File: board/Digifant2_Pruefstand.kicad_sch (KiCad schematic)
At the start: 58 parts, among them J0 VW ECU HARNESS, J1 12V BENCH IN, J2 IDLE VALVE N71, J3 OLED / UI I2C, Q1 2N7002, Q2 P-MOS -30V >=5A, Q3 2N7002, Q5 2N7002, SW1 PUSH, SW2 PUSH, SW3 PUSH, U1 INA226 (0x40), U2 MCP4728 (0x60), U3 INA226 (0x41), U4 AD9833, U5 Raspberry Pi Pico, U6 TS5A3159A, U7 TS5A3159A, U8 TS5A3159A, Y1 25MHz

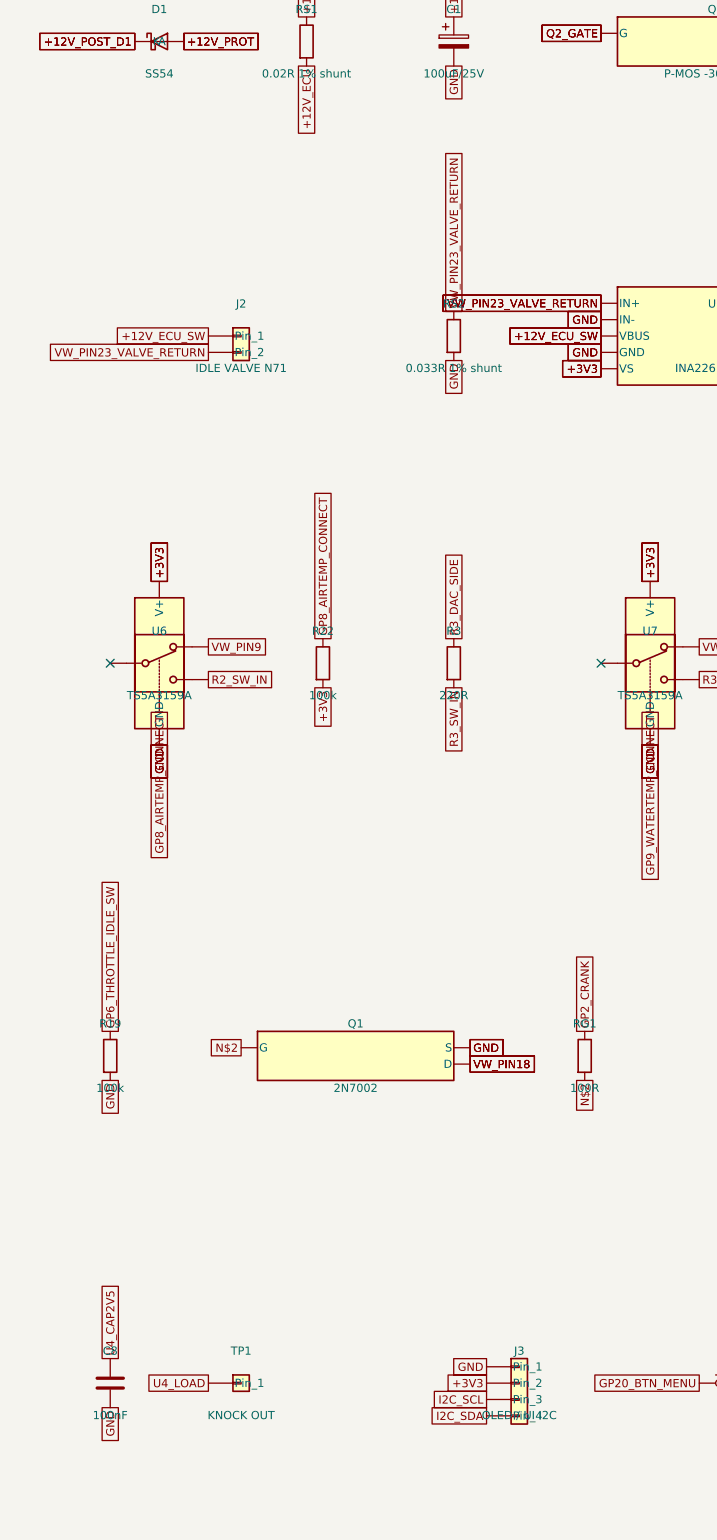
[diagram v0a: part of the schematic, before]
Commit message: Fix RS2's parallel ground path and give the knock output a real path out
Two of the three genuinely-open findings from USE_CASES.md:

1. RS2 (idle-valve shunt) sat as a separate tap to GND, in parallel with
   the ECU's own low-side driver on VW-23 -- both reached the same shared
   GND, so return current split between RS2 and the ECU's internal switch,
   and U3 only ever measured whatever fraction happened through RS2.
   Understated the true current, worst exactly when the ECU driver was on.
   Fixed: RS2 is now truly in series (valve -> RS2 -> VW-23), so 100% of
   the return current crosses it. U3's IN+/IN- assignment was swapped
   (IN+ keeps the net that already had a routed path to J0, IN- takes the
   new sense-side net) purely to minimize how much existing routing needed
   to change -- sign of the current reading is a firmware convention
   either way.

2. AD9833 knock output dead-ended at a single test pad with no path out.
   J0 is already full (15/15 positions; VW-4/5/7 were never broken out
   there), so this needed a separate small tap, same idea as J2 for the
   idle valve. A proper 2-pin JST connector was tried first (matching
   J2's style) but every placement attempt shorted a different existing
   net -- this corner of the board is threaded with +12V_ECU_SW,
   VW_PIN10/11/12, and GP8/GP9/GP13/GP26 on both layers. Used two small
   bare test pads (TP1 signal, TP2 ground, same footprint as the original
   TP1) instead, which fit where the connector wouldn't.

Both required real topology changes, not just added parts -- updated the
circuit source AND spliced the corresponding net-label renames into the
committed schematic (not just the PCB), otherwise a future PCB-from-
schematic sync would have silently reverted the RS2 fix.

One new residual, same class as the existing U1/U3/RS1/RS2 pocket: U3
pin 9's own local GND-mesh neighbours and its new sense-net connection
both need to route through the same tight spot. Tried by hand and via
Freerouting f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
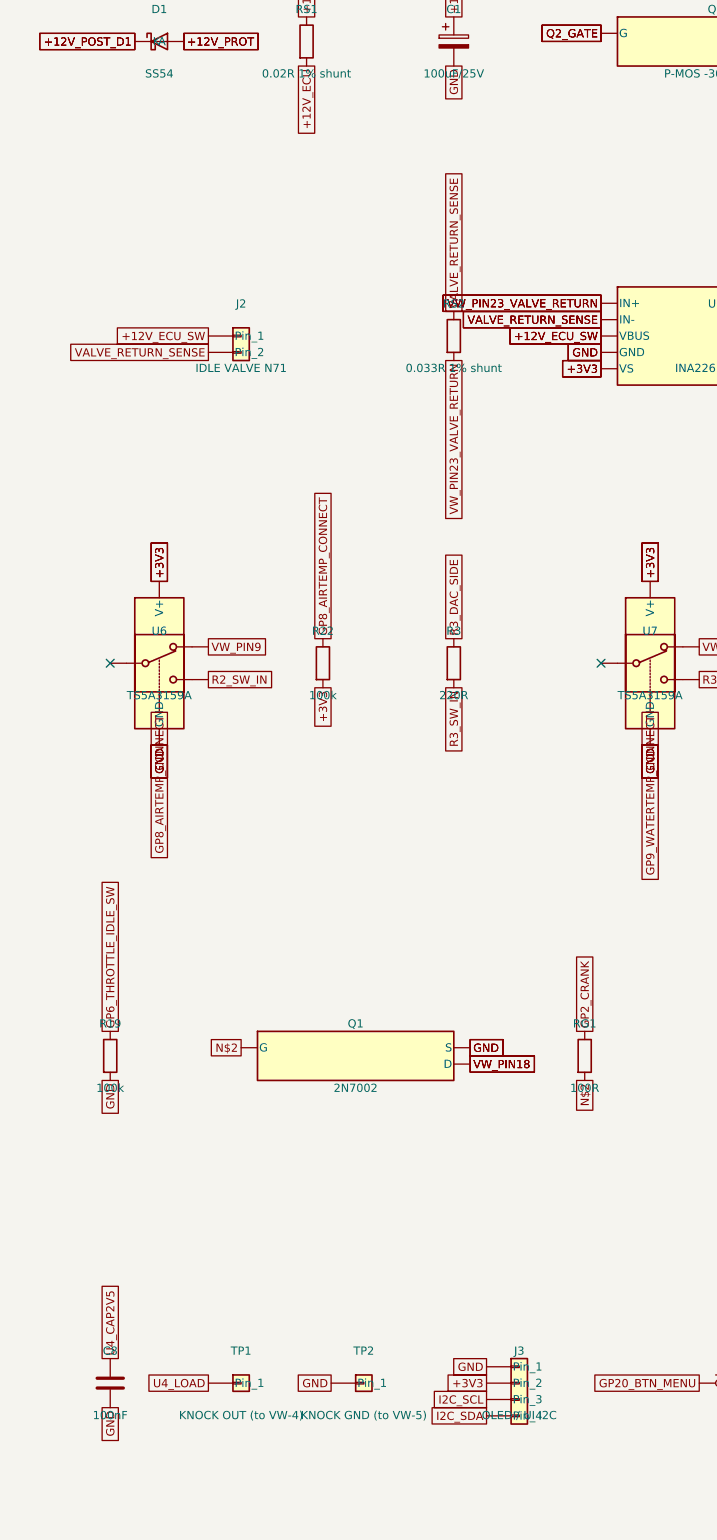
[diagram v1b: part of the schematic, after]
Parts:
- added TP2: KNOCK GND (to VW-5), TestPoint:TestPoint_Pad_D1.5mm, symbol Connector_Generic:Conn_01x01
- TP1: value KNOCK OUT -> KNOCK OUT (to VW-4)
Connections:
- net GND: now also TP2.1 (Pin_1); no longer RS2.2, U3.9 (IN-)
- net VW_PIN23_VALVE_RETURN: now also RS2.2; no longer J2.2 (Pin_2), RS2.1
- new net VALVE_RETURN_SENSE: J2.2 (Pin_2), RS2.1, U3.9 (IN-)
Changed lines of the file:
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@@
 		(property
 			"Value"
-			"KNOCK OUT"
+			"KNOCK OUT (to VW-4)"
 			(at 58.42 314.88 0)
 			(effects
@@
 			)
 		)
+		(symbol
+			(lib_id Connector_Generic:Conn_01x01)
+			(at 77.47 309.88 0)
+			(in_bom yes)
+			(on_board yes)
+			(dnp no)
+			(property
+				"Reference"
+				"TP2"
+				(at 77.47 304.88 0)
+				(effects
+					(font
+						(size 1.27 1.27)
+					)
+				)
+			)
+			(property
+				"Value"
+				"KNOCK GND (to VW-5)"
+				(at 77.47 314.88 0)
+				(effects
+					(font
+						(size 1.27 1.27)
+					)
+				)
+			)
+			(property
+				"Footprint"
+				"TestPoint:TestPoint_Pad_D1.5mm"
+				(at 77.47 319.88 0)
+				(effects
+					(font
+						(size 1.27 1.27)
+					)
+					(hide yes)
+				)
+			)
+			(instances
+				(project
+					"circuit"
+					(path
+						"/"
+						(reference TP2)
+						(unit 1)
+					)
+				)
+				(project
+					"/workspace/digifant2-pruefstand/digifant2_pruefstand_scratch_fix23/digifant2_pruefstand_scratch_fix23"
+					(path
+						"/1d0c82a2-feac-4989-ac41-75dbcafe7445/27b0ed1e-7c83-4569-a3b4-468bc8a85a9f"
+						(reference TP2)
+						(unit 1)
+					)
+				)
+			)
+		)
 	(global_label
 		VW_PIN2
@@
 	)
 	(global_label
-		GND
+		VW_PIN23_VALVE_RETURN
 		(at 91.44 151.13 270)
 		(effects
@@
 	)
 	(global_label
-		GND
+		VALVE_RETURN_SENSE
 		(at 114.30000000000001 144.78 180)
 		(effects
@@
 	)
 	(global_label
-		GND
+		VALVE_RETURN_SENSE
 		(at 114.30000000000001 144.78 180)
 		(effects
@@
 	)
 	(global_label
-		VW_PIN23_VALVE_RETURN
+		VALVE_RETURN_SENSE
 		(at 53.34 149.85999999999999 180)
 		(effects
@@
 	)
 	(global_label
-		VW_PIN23_VALVE_RETURN
+		VALVE_RETURN_SENSE
 		(at 91.44 143.51 90)
 		(effects
@@
 			(effects
 				(font
+					(size 1.27 1.27)
+				)
+				(justify right)
+			)
+		)
+		(global_label
+			GND
+			(at 72.39 309.88 180)
+			(effects
+				(font

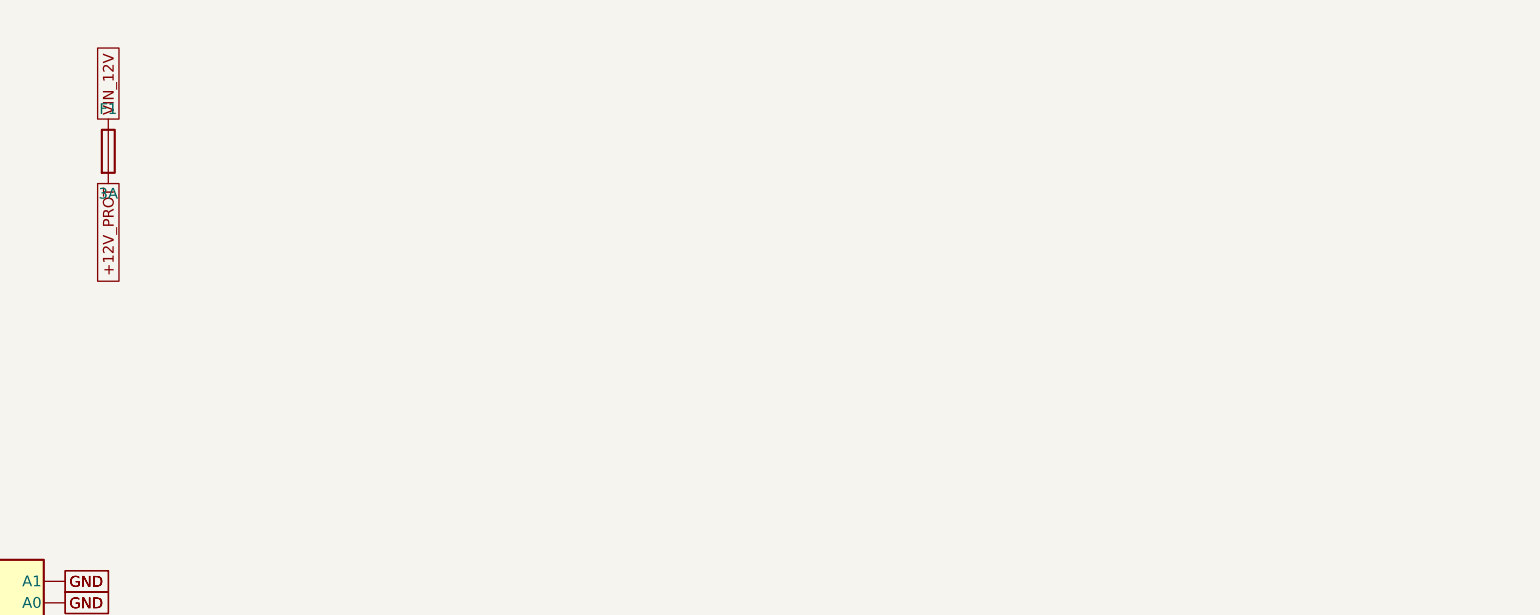
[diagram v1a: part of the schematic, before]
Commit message: Add 12 scope-probe test points (TP3-TP14) for firmware debugging
Bare 1.5mm test pads (same TestPoint_Pad_D1.5mm footprint as the knock
output's TP1/TP2) on the signals most likely to get probed while
debugging: crank drive, idle-switch drive, ignition/injector capture,
the AD9833 SPI bus (CS/SCK/MOSI), the I2C bus (SDA/SCL), the status LED
data line, and both 12V rails (sensed + switched).

Placement used an automated collision check (footprint + track distance)
against the real board, not manual trial and error -- 12 of 13 originally
attempted points cleared on the first or second pass. +3V3 was dropped
after 4 different anchor attempts (3 different Pico pins, then a
decoupling cap elsewhere) all routed through the same congested corridor
near the Pico; not worth forcing given +3V3 is already exposed at many
existing component pins.

Added digifant2_pruefstand.py's debug_test_points() and spliced the
corresponding schematic symbols/labels into the committed schematic
(verified ERC-clean and schematic-PCB parity unchanged from baseline) --
same lesson as the RS2 fix: a PCB-only addition would silently disappear
on the next schematic sync.

One real residual: TP12 (LED data) reopened a shorting_items/clearance
pair against GND. The actual pad-to-pad distances involved are ~2mm --
nowhere near a real clearance violation -- so the true conflict is
somewhere along the newly-routed copper itself, not locatable precisely
by script. Left for the same manual-nudge treatment as this board's
other tight pockets; KiCad's interactive router will show the exact
offending trace visually.

Co-Authored-By: Claude Sonnet 5 <noreply@anthropic.com>
Claude-Session: https://claude.ai/code/session_01XcEuUwwCT37oProAm8HYeY
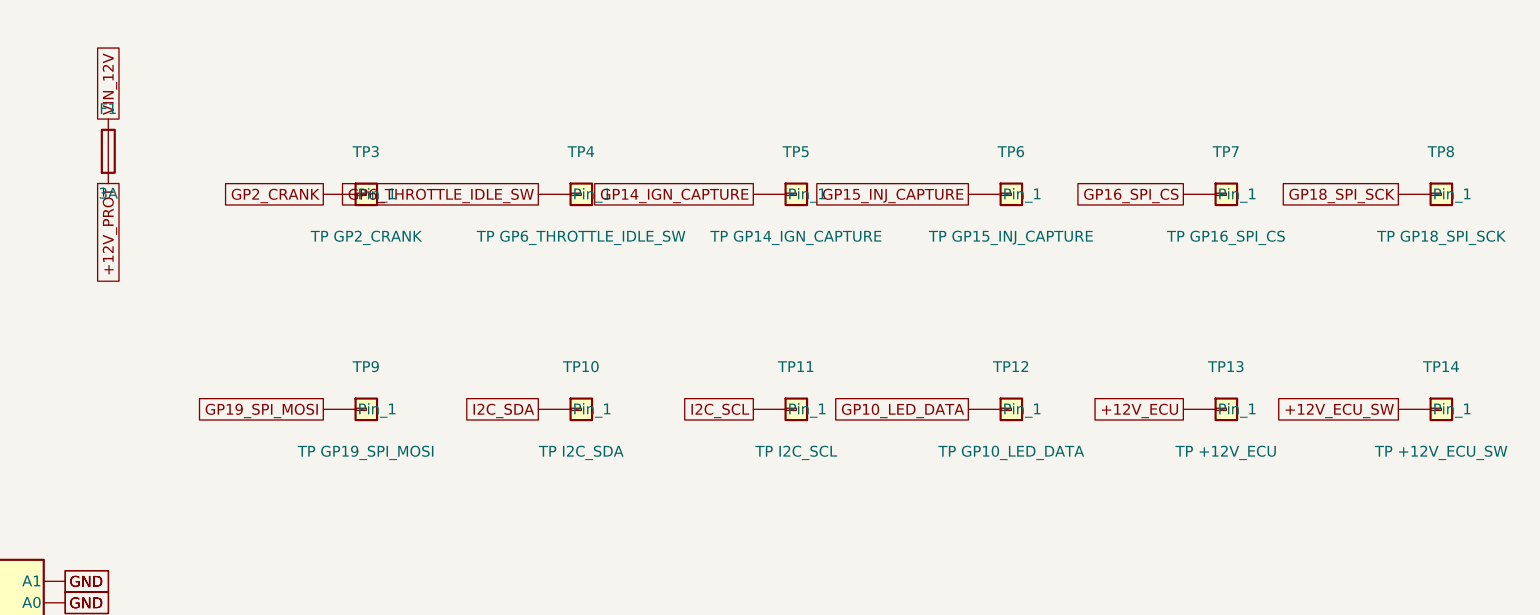
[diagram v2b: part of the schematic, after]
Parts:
- added TP10: TP I2C_SDA, TestPoint:TestPoint_Pad_D1.5mm, symbol Connector_Generic:Conn_01x01
- added TP11: TP I2C_SCL, TestPoint:TestPoint_Pad_D1.5mm, symbol Connector_Generic:Conn_01x01
- added TP12: TP GP10_LED_DATA, TestPoint:TestPoint_Pad_D1.5mm, symbol Connector_Generic:Conn_01x01
- added TP13: TP +12V_ECU, TestPoint:TestPoint_Pad_D1.5mm, symbol Connector_Generic:Conn_01x01
- added TP14: TP +12V_ECU_SW, TestPoint:TestPoint_Pad_D1.5mm, symbol Connector_Generic:Conn_01x01
- added TP3: TP GP2_CRANK, TestPoint:TestPoint_Pad_D1.5mm, symbol Connector_Generic:Conn_01x01
- added TP4: TP GP6_THROTTLE_IDLE_SW, TestPoint:TestPoint_Pad_D1.5mm, symbol Connector_Generic:Conn_01x01
- added TP5: TP GP14_IGN_CAPTURE, TestPoint:TestPoint_Pad_D1.5mm, symbol Connector_Generic:Conn_01x01
- added TP6: TP GP15_INJ_CAPTURE, TestPoint:TestPoint_Pad_D1.5mm, symbol Connector_Generic:Conn_01x01
- added TP7: TP GP16_SPI_CS, TestPoint:TestPoint_Pad_D1.5mm, symbol Connector_Generic:Conn_01x01
- added TP8: TP GP18_SPI_SCK, TestPoint:TestPoint_Pad_D1.5mm, symbol Connector_Generic:Conn_01x01
- added TP9: TP GP19_SPI_MOSI, TestPoint:TestPoint_Pad_D1.5mm, symbol Connector_Generic:Conn_01x01
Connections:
- net +12V_ECU: now also TP13.1 (Pin_1)
- net +12V_ECU_SW: now also TP14.1 (Pin_1)
- net GP10_LED_DATA: now also TP12.1 (Pin_1)
- net GP14_IGN_CAPTURE: now also TP5.1 (Pin_1)
- net GP15_INJ_CAPTURE: now also TP6.1 (Pin_1)
- net GP16_SPI_CS: now also TP7.1 (Pin_1)
- net GP18_SPI_SCK: now also TP8.1 (Pin_1)
- net GP19_SPI_MOSI: now also TP9.1 (Pin_1)
- net GP2_CRANK: now also TP3.1 (Pin_1)
- net GP6_THROTTLE_IDLE_SW: now also TP4.1 (Pin_1)
- net I2C_SCL: now also TP11.1 (Pin_1)
- net I2C_SDA: now also TP10.1 (Pin_1)

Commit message: Fix test points: real THT footprint, and move 10 out from under the Pico
Two real defects caught by user review of the previous commit:

1. All 14 test points (TP1-TP14) used TestPoint_Pad_D1.5mm, a bare SMD
   pad with no drill -- not THT as documented/intended. Switched to
   TestPoint_THTPad_D1.5mm_Drill0.7mm (real 0.7mm hole), vendored the
   footprint, and updated fetch_libs.sh.

2. TP3-TP12 were anchored right at their signal's own Pico pin, which
   placed 10 of the 12 physically *underneath* the Pico module's real
   footprint courtyard (x:[10,32.1] y:[47,99.1]) -- completely
   unreachable with a probe once the module is soldered on. Moved them
   to the clear margin strip west of the Pico (x=5mm), verified against
   real board-edge and courtyard geometry, not just pad/track proximity.

Along the way, found and fixed a real bug in this session's own PCB
scripts: pcbnew.FOOTPRINT(template) clones inherit the template's UUID
unless explicitly reset, so every footprint cloned this way (C7/C8, and
all of TP1-TP14, since they were all cloned from one template) shared a
UUID with its siblings. This doesn't break electrical connectivity but
corrupts DRC's item-identity tracking -- several "violations" this
session were real defects reported against the wrong footprint (one
report cited two parts 70mm apart as a courtyard overlap). Fixed with
ResetUuid() on every affected footprint and pad. With correct UUIDs,
DRC now correctly identified two genuine issues (TP1 too close to a
VW_PIN12 trace once it had a real drill hole; TP13's courtyard actually
overlapping RS1's) that had been reported against the wrong parts
before -- both repositioned and reverified.

Co-Authored-By: Claude Sonnet 5 <noreply@anthropic.com>
Claude-Session: https://claude.ai/code/session_01XcEuUwwCT37oProAm8HYeY
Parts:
- TP1, TP10, TP11, TP12, TP13, TP14, TP2, TP3, TP4, TP5, TP6, TP7, TP8, TP9: footprint TestPoint:TestPoint_Pad_D1.5mm -> TestPoint:TestPoint_THTPad_D1.5mm_Drill0.7mm
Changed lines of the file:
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@@
 		(property
 			"Footprint"
-			"TestPoint:TestPoint_Pad_D1.5mm"
+			"TestPoint:TestPoint_THTPad_D1.5mm_Drill0.7mm"
 			(at 58.42 319.88 0)
 			(effects
@@
 			(property
 				"Footprint"
-				"TestPoint:TestPoint_Pad_D1.5mm"
+				"TestPoint:TestPoint_THTPad_D1.5mm_Drill0.7mm"
 				(at 77.47 319.88 0)
 				(effects
@@
 			(property
 				"Footprint"
-				"TestPoint:TestPoint_Pad_D1.5mm"
+				"TestPoint:TestPoint_THTPad_D1.5mm_Drill0.7mm"
 				(at 396.24 60.80000000000001 0)
 				(effects
@@
 			(property
 				"Footprint"
-				"TestPoint:TestPoint_Pad_D1.5mm"
+				"TestPoint:TestPoint_THTPad_D1.5mm_Drill0.7mm"
 				(at 421.64 60.80000000000001 0)
 				(effects
@@
 			(property
 				"Footprint"
-				"TestPoint:TestPoint_Pad_D1.5mm"
+				"TestPoint:TestPoint_THTPad_D1.5mm_Drill0.7mm"
 				(at 447.04 60.80000000000001 0)
 				(effects
@@
 			(property
 				"Footprint"
-				"TestPoint:TestPoint_Pad_D1.5mm"
+				"TestPoint:TestPoint_THTPad_D1.5mm_Drill0.7mm"
 				(at 472.44 60.80000000000001 0)
 				(effects
@@
 			(property
 				"Footprint"
-				"TestPoint:TestPoint_Pad_D1.5mm"
+				"TestPoint:TestPoint_THTPad_D1.5mm_Drill0.7mm"
 				(at 497.84000000000003 60.80000000000001 0)
 				(effects
@@
 			(property
 				"Footprint"
-				"TestPoint:TestPoint_Pad_D1.5mm"
+				"TestPoint:TestPoint_THTPad_D1.5mm_Drill0.7mm"
 				(at 523.24 60.80000000000001 0)
 				(effects
@@
 			(property
 				"Footprint"
-				"TestPoint:TestPoint_Pad_D1.5mm"
+				"TestPoint:TestPoint_THTPad_D1.5mm_Drill0.7mm"
 				(at 396.24 86.19999999999999 0)
 				(effects
@@
 			(property
 				"Footprint"
-				"TestPoint:TestPoint_Pad_D1.5mm"
+				"TestPoint:TestPoint_THTPad_D1.5mm_Drill0.7mm"
 				(at 421.64 86.19999999999999 0)
 				(effects
@@
 			(property
 				"Footprint"
-				"TestPoint:TestPoint_Pad_D1.5mm"
+				"TestPoint:TestPoint_THTPad_D1.5mm_Drill0.7mm"
 				(at 447.04 86.19999999999999 0)
 				(effects
@@
 			(property
 				"Footprint"
-				"TestPoint:TestPoint_Pad_D1.5mm"
+				"TestPoint:TestPoint_THTPad_D1.5mm_Drill0.7mm"
 				(at 472.44 86.19999999999999 0)
 				(effects
@@
 			(property
 				"Footprint"
-				"TestPoint:TestPoint_Pad_D1.5mm"
+				"TestPoint:TestPoint_THTPad_D1.5mm_Drill0.7mm"
 				(at 497.84000000000003 86.19999999999999 0)
 				(effects
@@
 			(property
 				"Footprint"
-				"TestPoint:TestPoint_Pad_D1.5mm"
+				"TestPoint:TestPoint_THTPad_D1.5mm_Drill0.7mm"
 				(at 523.24 86.19999999999999 0)
 				(effects
